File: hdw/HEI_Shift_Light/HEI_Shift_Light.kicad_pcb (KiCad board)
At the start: 4 copper layers, 70.7 x 56.9 mm, 112 parts, among them J201 VIN, J401 TACH, J501 PICKIT4, J601 USB_C_Receptacle_USB2.0_16P, Q301 DMN3150LW-7, Q302 DMN3150LW-7, Q701 DMN3150LW-7, Q702 DMN3150LW-7, Q703 DMN3150LW-7, U201 TPS26624DRCR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

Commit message: finished routing
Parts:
- removed the H814 at (3.08, 3.08)
- renumbered H804 to H814
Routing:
- net I2C_SDA: track 1.75 -> 26.7 mm, vias 1 -> 2
- net I2C_SCL: track 1.70 -> 24.6 mm, vias 1 -> 2
- net GND: track 49.8 -> 65.8 mm
- net TACH_ANALOG: track 27.9 -> 27.3 mm

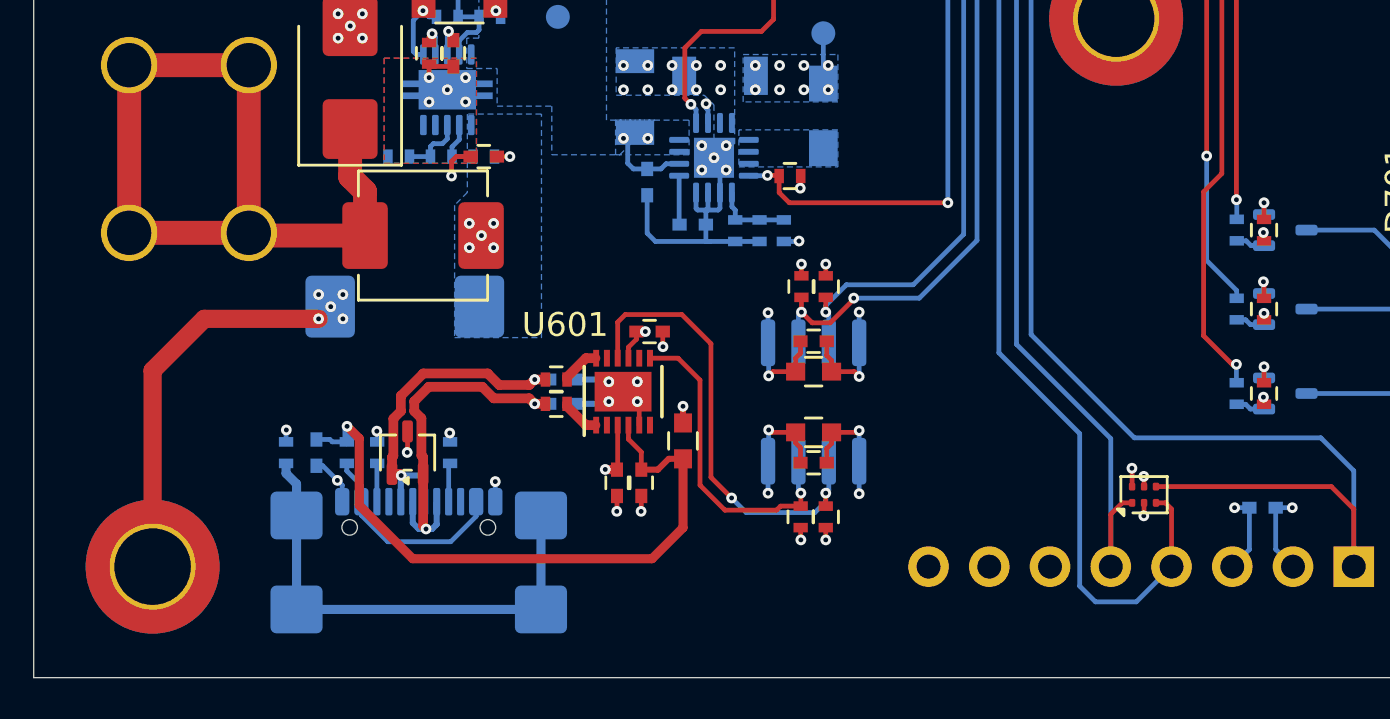
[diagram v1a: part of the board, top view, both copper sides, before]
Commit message: added silkscreen project description, DRC checks
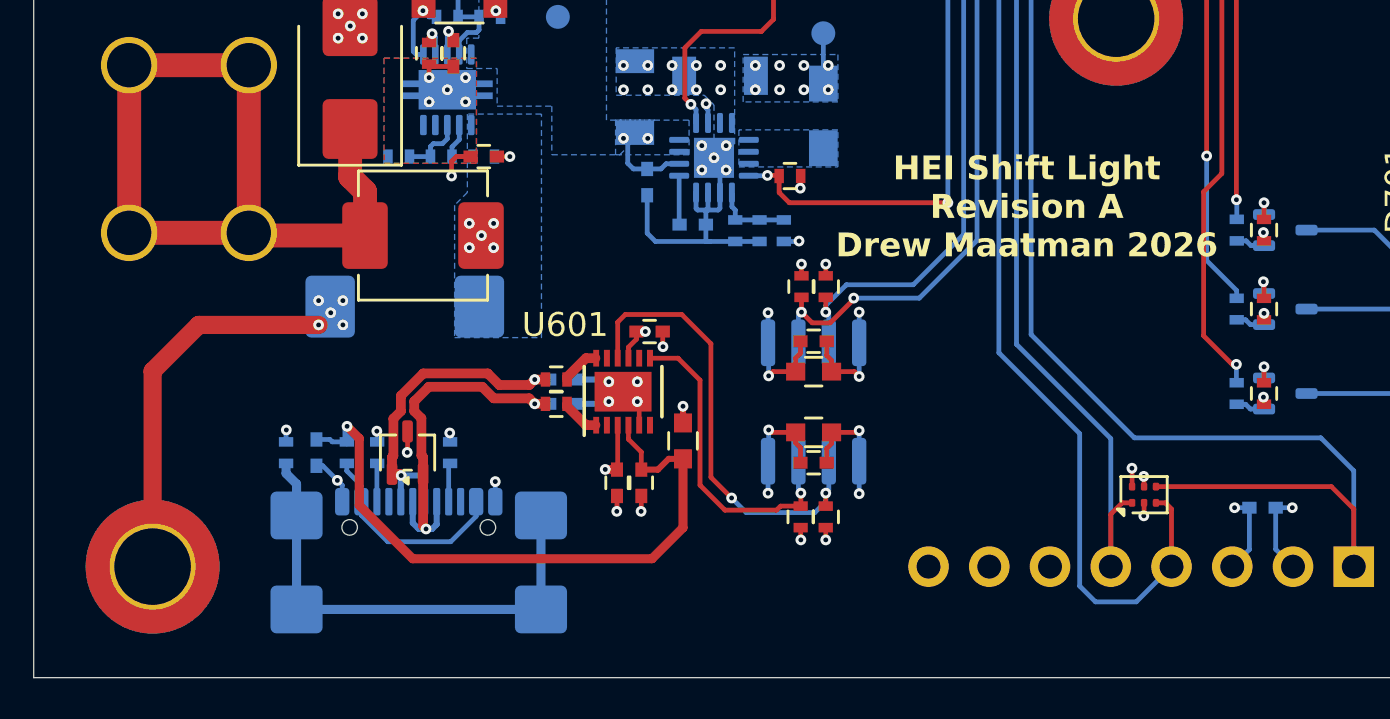
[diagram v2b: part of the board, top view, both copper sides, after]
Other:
- board text added: "HEI Shift Light Revision A Drew Maatman 2026"
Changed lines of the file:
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@@
 		(layer "User.4")
+	)
+	(gr_text "HEI Shift Light\nRevision A\nDrew Maatman 2026"
+		(at 136.5504 96.901 0)
+		(layer "F.SilkS")
+		(effects
+			(font
+				(size 1 1)
+				(thickness 0.2)
+				(bold yes)
+			)
+			(justify bottom)
+		)
 	)
 	(gr_text "PICKIT4"
@@
 	)
 	(segment
+		(start 99.99654 101.57786)
+		(end 101.92713 99.64727)
+		(width 0.762)
+		(layer "F.Cu")
+		(net "GND")
+	)
+	(segment
 		(start 122.543 70.358)
 		(end 123.444 70.358)
@@
 	)
 	(segment
+		(start 101.92713 99.64727)
+		(end 106.937237 99.64727)
+		(width 0.762)
+		(layer "F.Cu")
+		(net "GND")
+	)
+	(segment
 		(start 146.46845 97.8662)
 		(end 146.44305 97.8408)
@@
 	)
 	(segment
-		(start 99.99654 101.55246)
-		(end 102.15573 99.39327)
-		(width 0.762)
-		(layer "F.Cu")
-		(net "GND")
-	)
-	(segment
 		(start 129.1351 84.6597)
 		(end 129.1844 84.709)
@@
 	)
 	(segment
+		(start 99.99654 109.7534)
+		(end 99.99654 101.57786)
+		(width 0.762)
+		(layer "F.Cu")
+		(net "GND")
+	)
+	(segment
 		(start 112.4966 92.8116)
 		(end 112.4966 93.4212)
@@
 	)
 	(segment
-		(start 99.99654 109.7534)
-		(end 99.99654 101.55246)
-		(width 0.762)
-		(layer "F.Cu")
-		(net "GND")
-	)
-	(segment
 		(start 128.385 101.6)
 		(end 128.385 101.1308)
@@
 	)
 	(segment
-		(start 102.15573 99.39327)
-		(end 106.937237 99.39327)
-		(width 0.762)
-		(layer "F.Cu")
-		(net "GND")
-	)
-	(segment
 		(start 141.4514 107.087)
 		(end 141.4514 107.6194)
@@
 	)
 	(via
-		(at 107.445237 98.88527)
+		(at 107.445237 99.13927)
 		(size 0.45)
 		(drill 0.2)
@@
 	)
 	(via
-		(at 106.937237 99.39327)
+		(at 106.937237 99.64727)
 		(size 0.45)
 		(drill 0.2)
@@
 	)
 	(via
-		(at 107.953237 98.37727)
+		(at 107.953237 98.63127)
 		(size 0.45)
 		(drill 0.2)
@@
 	)
 	(via
-		(at 107.953237 99.39327)
+		(at 107.953237 99.64727)
 		(size 0.45)
 		(drill 0.2)
@@
 	)
 	(via
-		(at 106.937237 98.37727)
-		(size 0.45)
-		(drill 0.2)
+		(at 106.937237 98.63127)
+		(size 0.45)
+		(drill 0.2)
